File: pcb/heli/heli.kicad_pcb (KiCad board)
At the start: 4 copper layers, 50.6 x 50 mm, 71 parts, among them J1 Batterie, J2 Debug, J3 CONMHF4-SMD-G-T, J4 Servo, J5 Servo, M1 Motor_DC, M2 Motor_DC, Q1 IRLZ44N, Q2 BC547, Q3 IRLZ44N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

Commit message: 
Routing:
- net GND: vias 121 -> 123
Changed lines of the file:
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@@
   (via (at 43.688 17.018) (size 0.5) (drill 0.25) (layers "F.Cu" "B.Cu") (free) (net 2))
   (via (at 49.6 62.02) (size 0.5) (drill 0.25) (layers "F.Cu" "B.Cu") (free) (net 2))
+  (via (at 61.17 47.22) (size 0.5) (drill 0.25) (layers "F.Cu" "B.Cu") (free) (net 2))
   (via (at 55.311168 26.333969) (size 0.5) (drill 0.25) (layers "F.Cu" "B.Cu") (free) (net 2))
   (via (at 40.9448 39.6748) (size 0.5) (drill 0.25) (layers "F.Cu" "B.Cu") (free) (net 2))
@@
   (via (at 63.1444 45.7708) (size 0.5) (drill 0.25) (layers "F.Cu" "B.Cu") (free) (net 2))
   (via (at 44.3992 17.526) (size 0.5) (drill 0.25) (layers "F.Cu" "B.Cu") (free) (net 2))
+  (via (at 50.47 36.53) (size 0.5) (drill 0.25) (layers "F.Cu" "B.Cu") (free) (net 2))
   (via (at 65.6 38.025) (size 0.5) (drill 0.25) (layers "F.Cu" "B.Cu") (free) (net 2))
   (via (at 63.7032 32.1056) (size 0.5) (drill 0.25) (layers "F.Cu" "B.Cu") (free) (net 2))

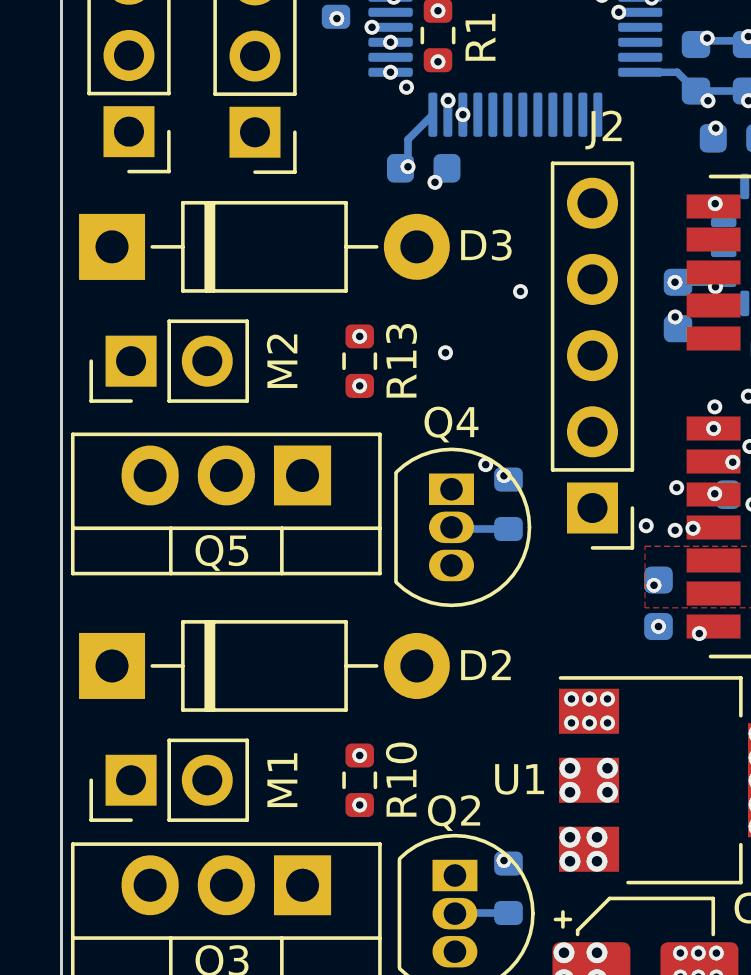
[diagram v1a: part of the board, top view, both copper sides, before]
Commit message: 
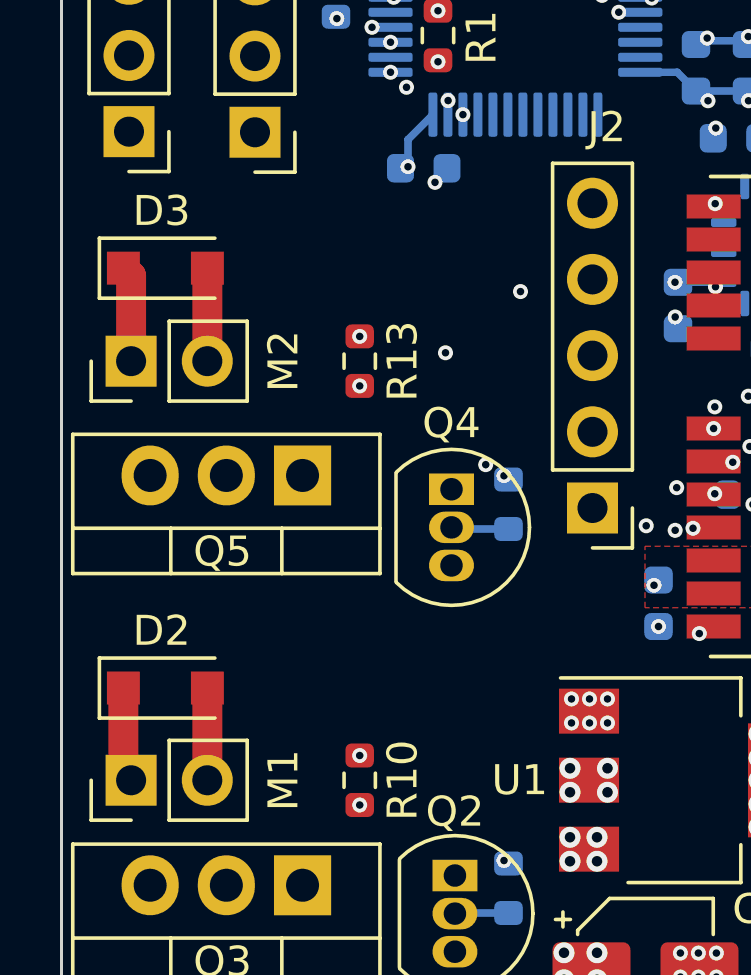
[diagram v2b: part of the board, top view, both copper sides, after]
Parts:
- C17, C20: value 22pF -> 30pF
- D2, D3: footprint Diode_THT:D_DO-41_SOD81_P10.16mm_Horizontal -> Diode_SMD:D_SOD-123F
- R4: value 170 -> 70
- moved D2 1.92 mm to (21.5, 47.7)
- moved D3 1.91 mm to (21.5, 33.7)
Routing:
- net 7.4V: track 0.11 -> 6.50 mm
- net Net-(D2-Pad2): track 12.3 -> 6.84 mm
- net Net-(D3-Pad2): track 12.6 -> 7.17 mm

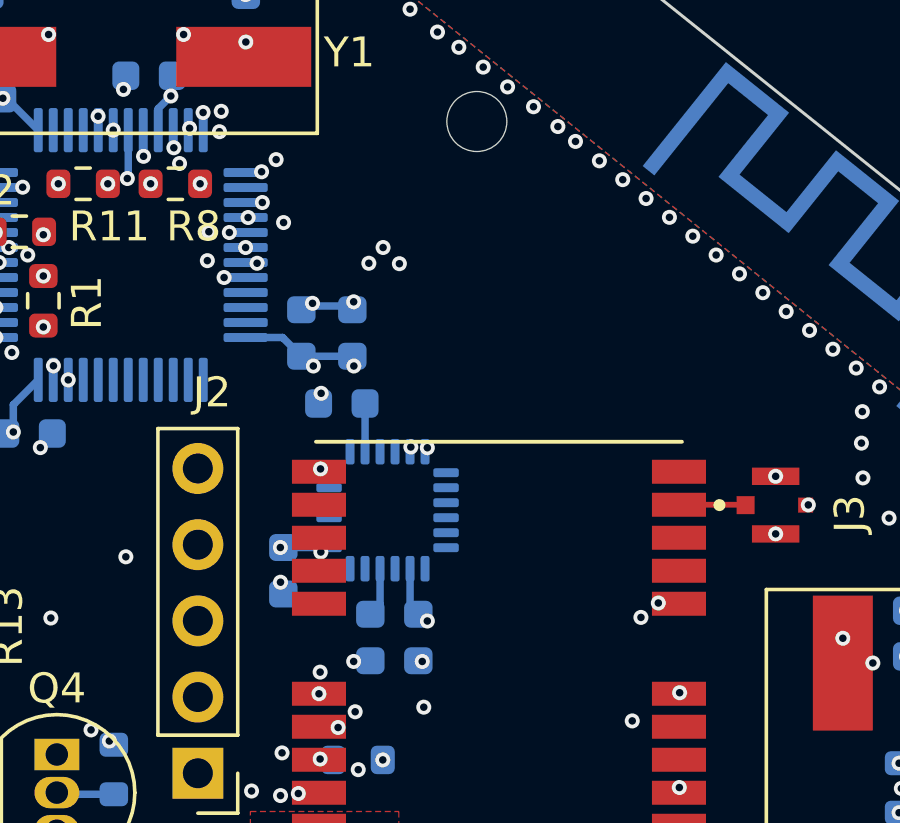
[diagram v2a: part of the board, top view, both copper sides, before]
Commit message: 
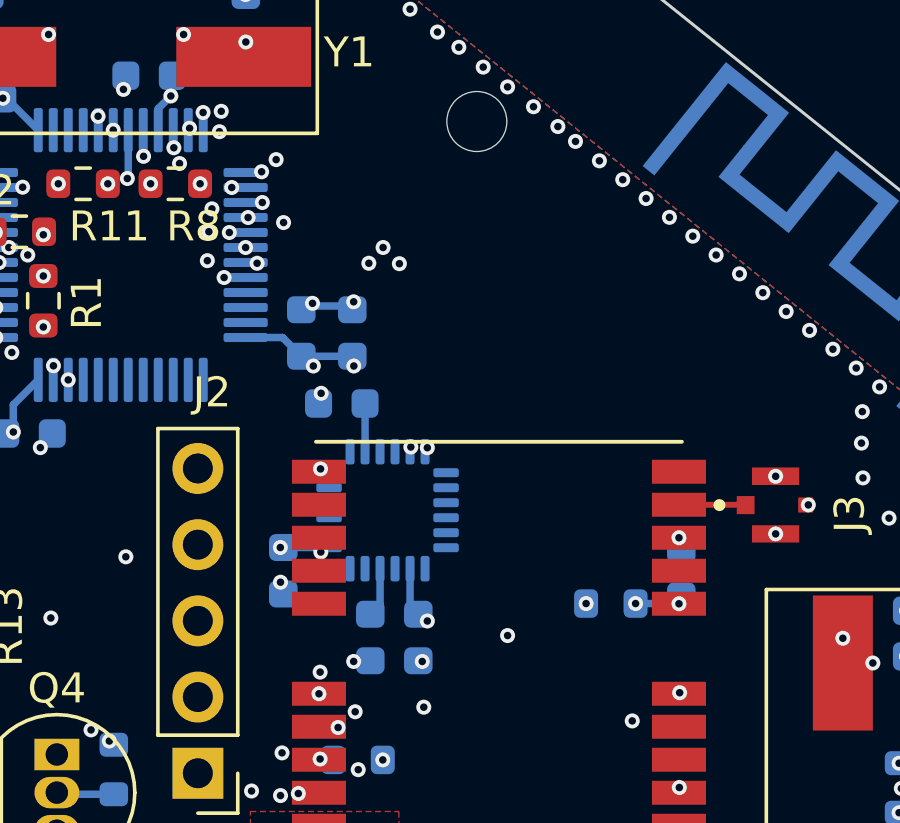
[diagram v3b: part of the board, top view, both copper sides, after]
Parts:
- added C27: 100nF, Capacitor_SMD:C_0603_1608Metric, B.Cu at (51.8, 35.0)
- added R15: 10k, Resistor_SMD:R_0603_1608Metric, B.Cu at (49.5, 36.1)
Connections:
- U3 pad 14: unconnected-(U3-Pad14) -> GPS_NRST
- U4 pad 8: RESET -> GPS_NRST
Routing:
- net GPS_NRST: track 0.00 -> 24.4 mm, vias 0 -> 3
- net RESET: track 65.1 -> 60.7 mm
- net GND: vias 123 -> 125
- net 3.3V: vias 43 -> 44

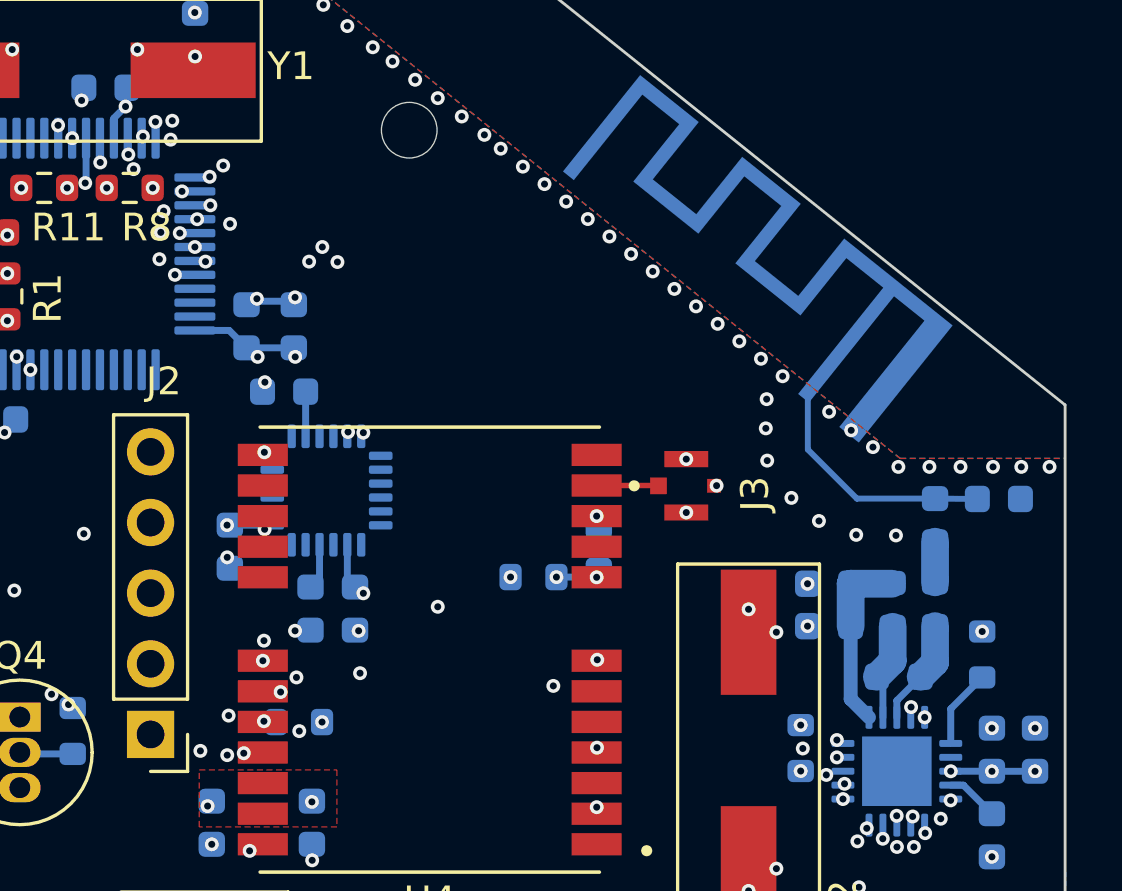
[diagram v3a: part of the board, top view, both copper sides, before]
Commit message: 
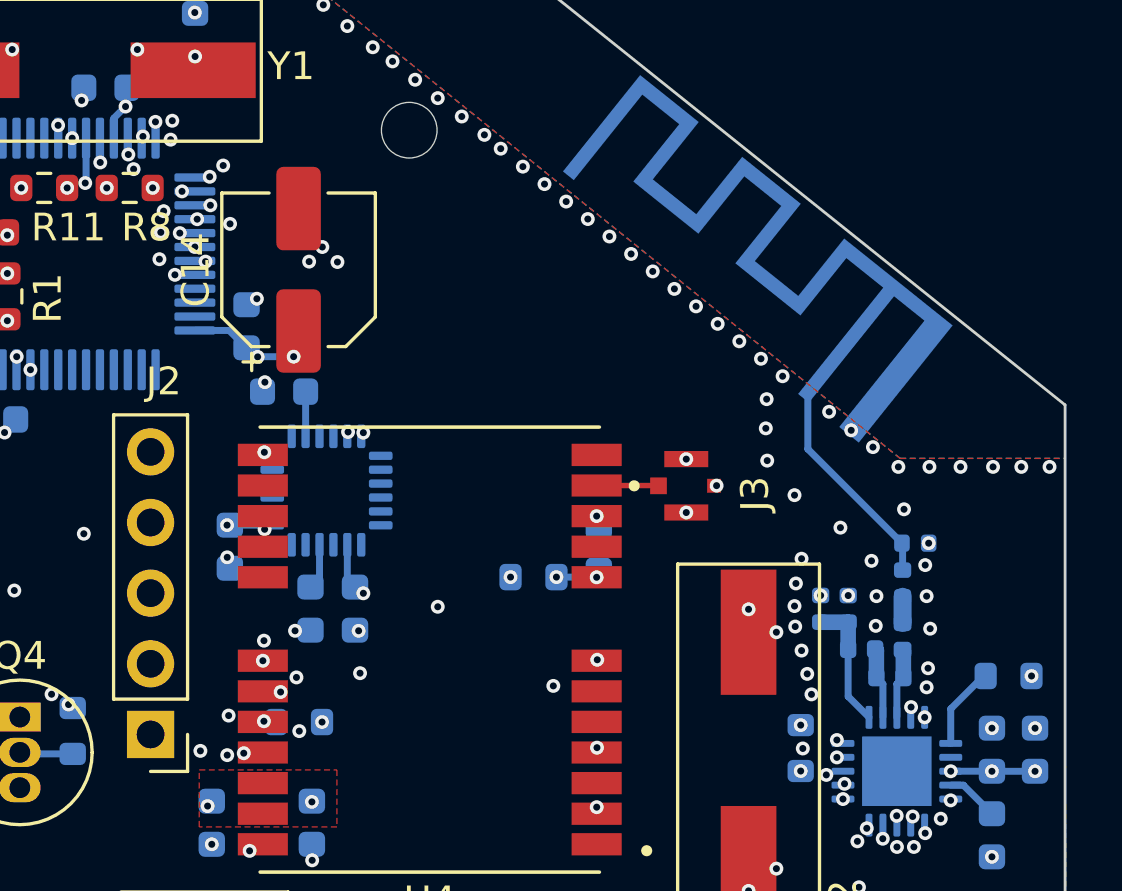
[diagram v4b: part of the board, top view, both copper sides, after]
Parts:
- C14: footprint Capacitor_SMD:C_0603_1608Metric -> Capacitor_SMD:CP_Elec_5x5.9; moved to F.Cu
- C18, C19, C21, C22: footprint Capacitor_SMD:C_0603_1608Metric -> Capacitor_SMD:C_0402_1005Metric
- C4, C5: value 0.1uF -> 100nF
- L1, L2, L3: footprint Inductor_SMD:L_0603_1608Metric -> Inductor_SMD:L_0402_1005Metric
- moved C22 3.40 mm to (63.2, 34.8)
- moved C21 2.56 mm to (62.7, 36.3)
- moved C14 2.04 mm to (41.0, 25.0)
- moved L2 1.94 mm to (61.3, 38.7), turned to 180 degrees
- moved L3 1.64 mm to (62.7, 38.2)
- moved R3 1.22 mm to (66.5, 39.6), turned to 180 degrees
- moved C18 0.95 mm to (59.8, 37.2), turned to -90 degrees
- moved C19 0.93 mm to (60.8, 37.2), turned to -90 degrees
- moved L1 0.32 mm to (62.3, 39.7)
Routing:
- net Net-(C18-Pad2): track 6.60 -> 4.72 mm
- net GND: track 1.66 -> 0.04 mm, vias 125 -> 139
- net Net-(L1-Pad2): track 3.85 -> 2.53 mm
- net /Radio/50ohm: track 8.86 -> 7.78 mm
- net Net-(L1-Pad1): track 3.58 -> 2.57 mm
- net Net-(C21-Pad1): track 1.46 -> 0.94 mm

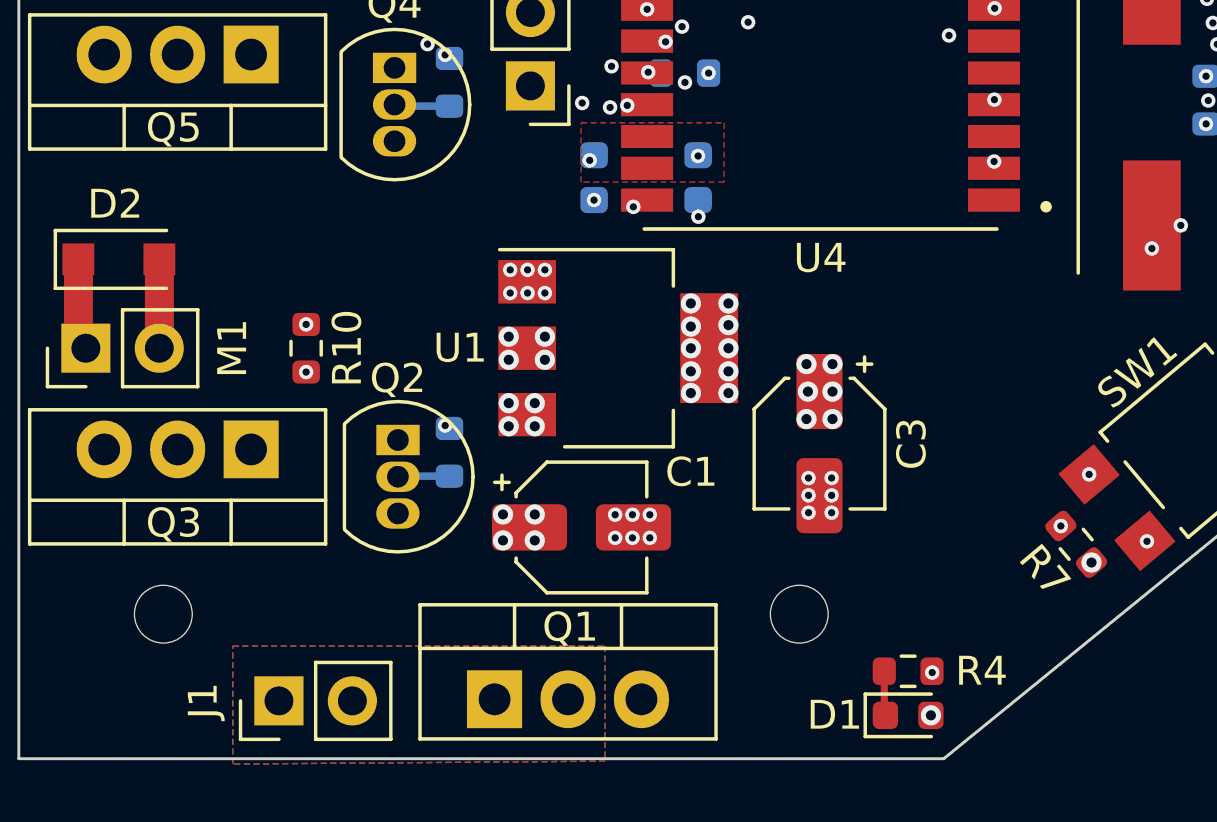
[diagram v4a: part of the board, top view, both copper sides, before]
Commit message: 
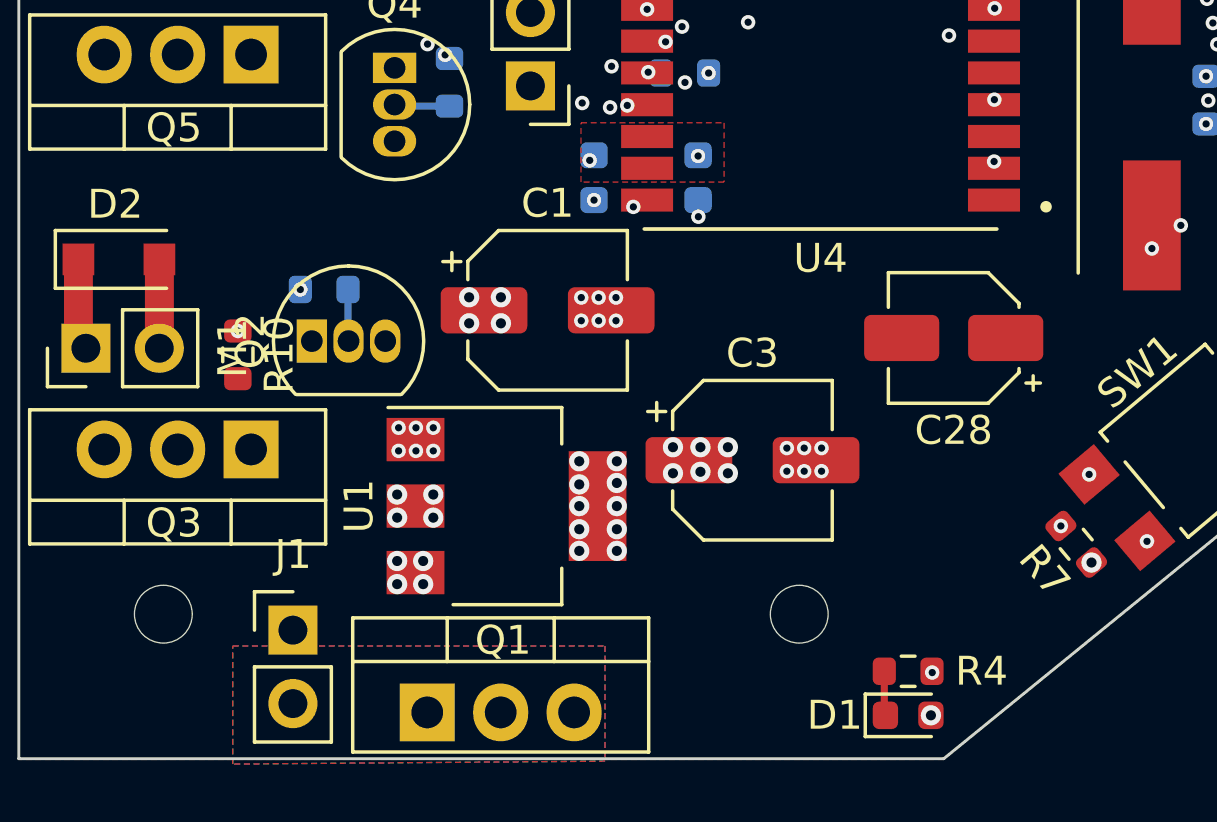
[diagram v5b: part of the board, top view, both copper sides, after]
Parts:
- added C28: 1uF, Capacitor_SMD:CP_Elec_4x5.4, F.Cu at (50.3, 50.4)
- C1, C3: footprint Capacitor_SMD:CP_Elec_4x5.4 -> Capacitor_SMD:CP_Elec_5x5.4
- moved C1 7.60 mm to (36.3, 49.5)
- moved R9 7.11 mm to (28.6, 48.8), turned to 0 degrees
- moved U1 6.69 mm to (34.9, 56.3)
- moved Q2 4.54 mm to (28.1, 50.6), turned to 0 degrees
- moved J1 2.49 mm to (27.5, 60.6), turned to 0 degrees
- moved C3 2.39 mm to (43.4, 54.7), turned to 0 degrees
- moved R10 2.37 mm to (25.6, 51.0)
- moved Q1 2.37 mm to (32.1, 63.4)
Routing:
- net Net-(Q2-Pad1): track 8.68 -> 0.46 mm, vias 1 -> 0
- net /PWM1: track 33.5 -> 32.1 mm
- net 3.3V: track 18.7 -> 17.5 mm
